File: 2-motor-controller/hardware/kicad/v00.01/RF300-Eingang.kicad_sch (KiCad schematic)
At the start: 7 parts, among them Q3 BC337

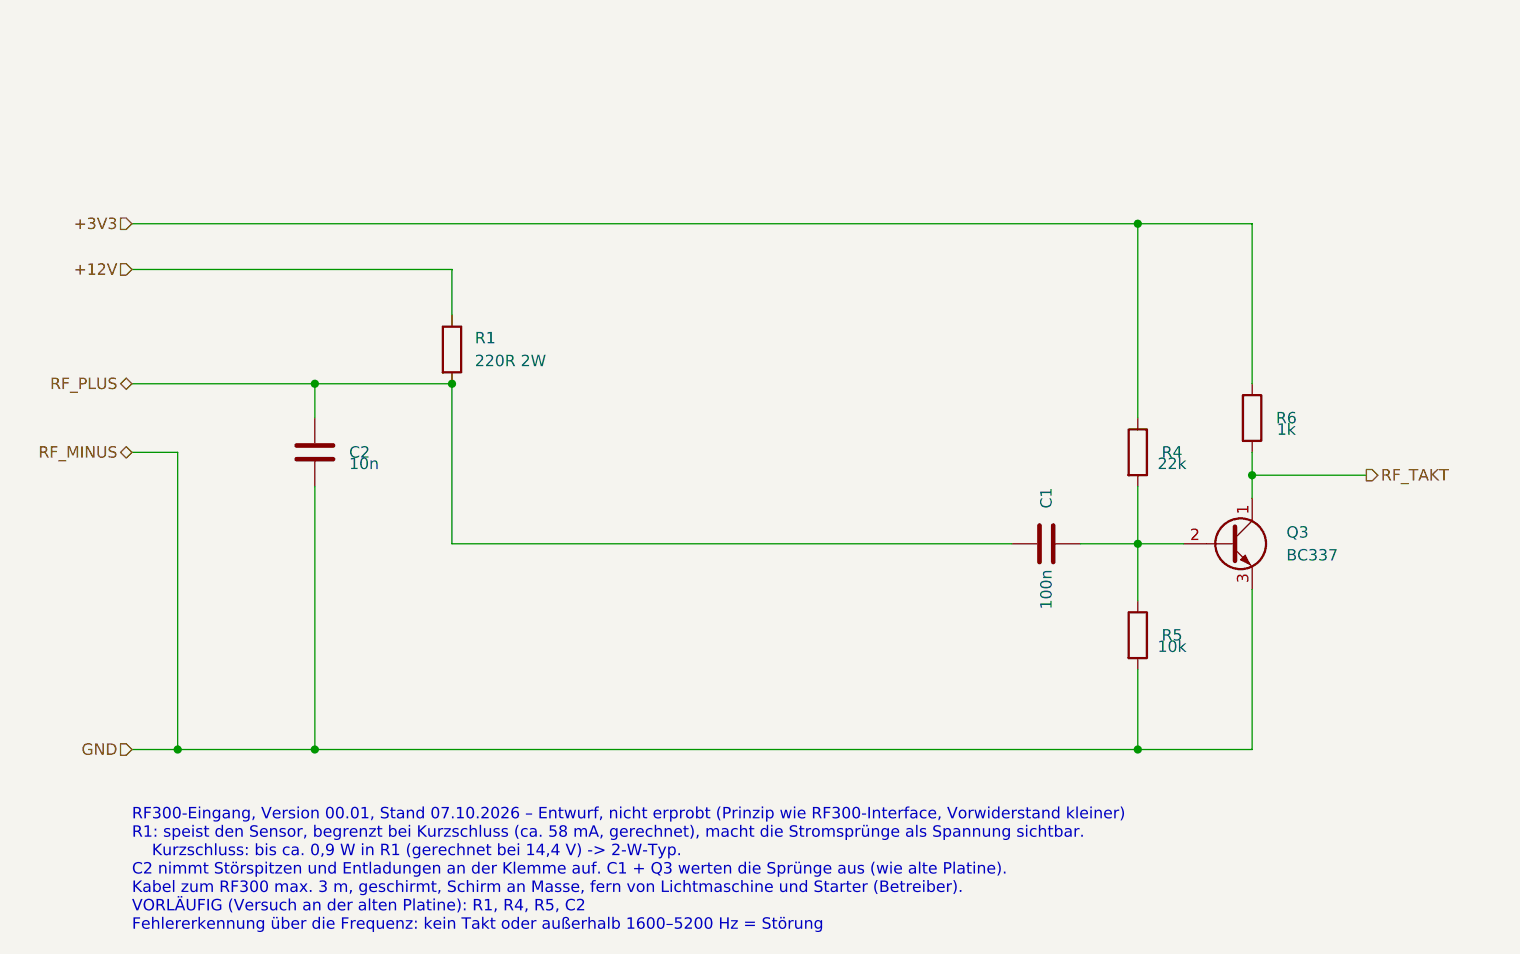
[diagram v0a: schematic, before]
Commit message: Motor-Controller: alle Blaetter nach den Zeichenregeln (Rahmen, Gruppen), 5-V-Zweig mit 2 x 4,7 uF, Titelfelder Version 00.01; Pruefung gegen Blockschaltbild 78/78
Co-Authored-By: Claude Opus 5.5 <noreply@anthropic.com>
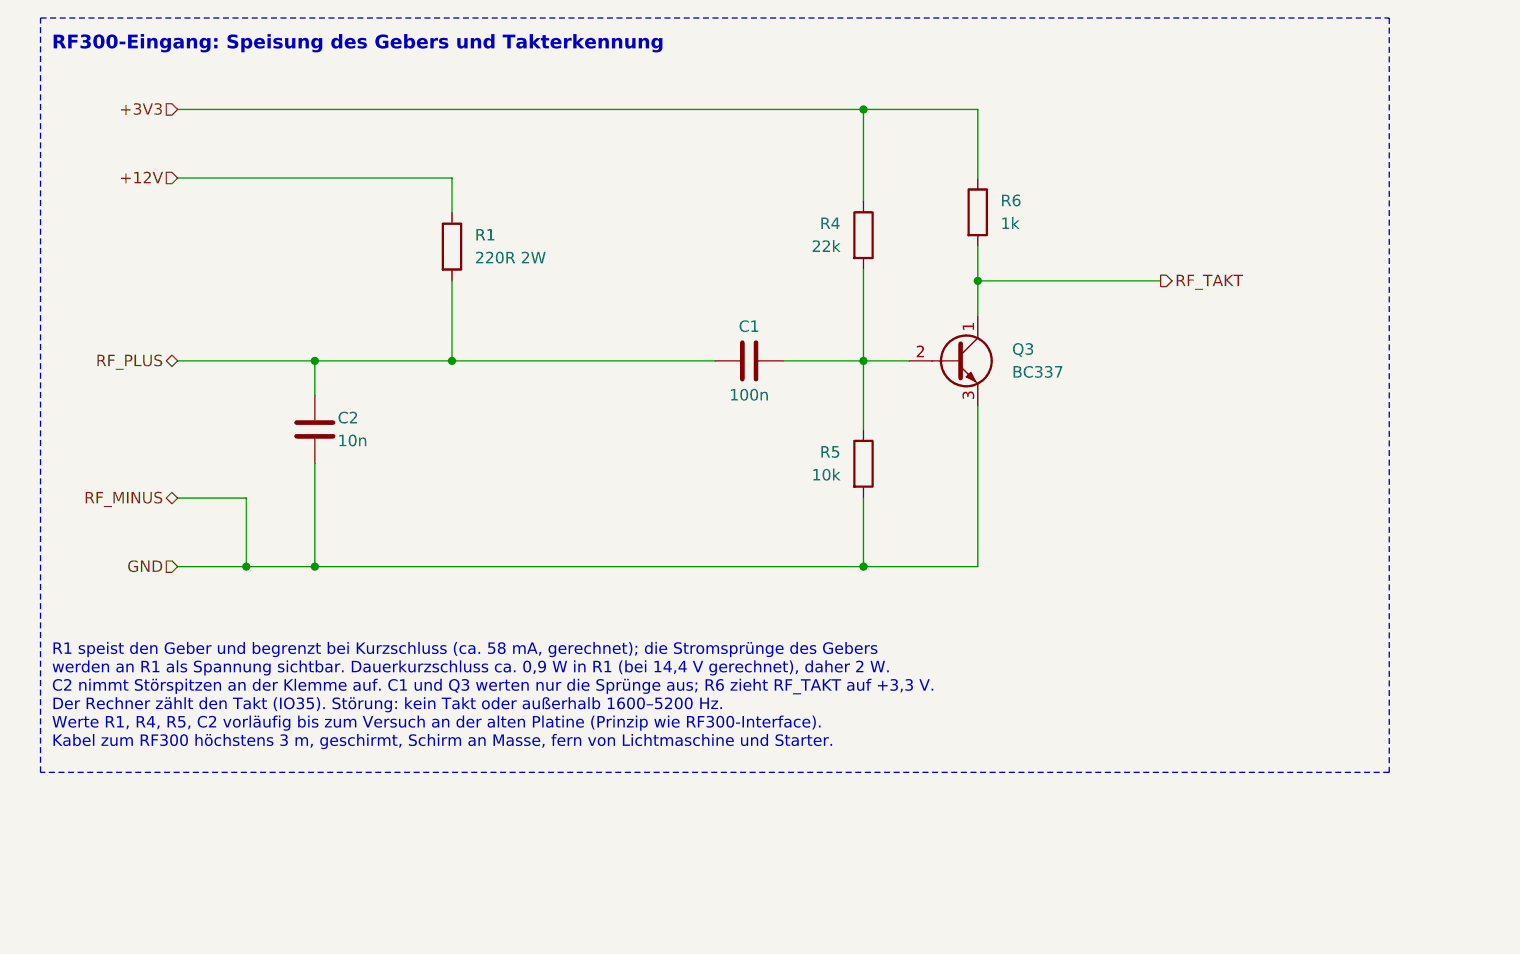
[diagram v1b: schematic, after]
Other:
- note added: "R1 speist den Geber und begrenzt bei Kurzschluss (ca. 58 mA, gerechnet); die Stromsprünge des Gebers werden an R1 als Spannung sichtbar. Dauerkurzschluss ca. 0,9 W in R1 (bei 14,4 V gerechnet), daher 2 W. C2 nimmt Störspitzen an der Klemme auf. C1 und Q3 werten nur die Sprünge aus; R6 zieht RF_TAKT auf +3,3 V. Der Rechner zählt den Takt (IO35). Störung: kein Takt oder außerhalb 1600–5200 Hz. Wert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"
- note added: "RF300-Eingang: Speisung des Gebers und Takterkennung"
- note removed: "RF300-Eingang, Version 00.01, Stand 07.10.2026 – Entwurf, nicht erprobt (Prinzip wie RF300-Interface, Vorwiderstand kleiner) R1: speist den Sensor, begrenzt bei Kurzschluss (ca. 58 mA, gerechnet), macht die Stromsprünge als Spannung sichtbar. Kurzschluss: bis ca. 0,9 W in R1 (gerechnet bei 14,4 V) -> 2-W-Typ. C2 nimmt Störspitzen und Entladungen an der Klemme auf. C1 + Q3 werten die Sprünge aus (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"
- company: (none) -> SuAn-Autopilot-Projekt
- title: (none) -> Motor-Controller V2.0 – RF300-Eingang

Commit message: Motor-Controller: Loetbilder zugeordnet (eigene: Dialight 551, TL1105, KEMET C320, Display-Leiste), Platine 150 x 130 mm mit allen 94 Teilen angeordnet - Bauteilauswahl 00.23, Anforderungen 00.11, Stueckliste 00.19
Co-Authored-By: Claude Opus 5.5 <noreply@anthropic.com>
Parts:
- C1, C2: footprint Capacitor_THT:C_Disc_D5.0mm_W2.5mm_P5.00mm -> Motor-Controller:C_KEMET_C320_L5.1mm_W4.1mm_P2.54mm
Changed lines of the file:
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@@
 			)
 		)
-		(property "Footprint" "Capacitor_THT:C_Disc_D5.0mm_W2.5mm_P5.00mm"
+		(property "Footprint" "Motor-Controller:C_KEMET_C320_L5.1mm_W4.1mm_P2.54mm"
 			(at 45.72 86.36 0)
 			(hide yes)
@@
 			)
 		)
-		(property "Footprint" "Capacitor_THT:C_Disc_D5.0mm_W2.5mm_P5.00mm"
+		(property "Footprint" "Motor-Controller:C_KEMET_C320_L5.1mm_W4.1mm_P2.54mm"
 			(at 93.98 78.74 0)
 			(hide yes)
